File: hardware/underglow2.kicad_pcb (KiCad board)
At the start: 4 copper layers, 60 x 55 mm, 85 parts, among them J101 Conn_ST_STDC14, J102 ZE05H-16DP-2H, Q101 AO3401A, Q102 AO3400A, Q103 AO3400A, Q104 AO3400A, U101 ESP32-C3FH4, U102 SN65HVD230, U103 AMS1117-3.3, Y101 40_Mhz

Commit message: updates
Signed-off-by: Connor Rigby <connorr@hey.com>
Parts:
- added J104: FH34SRJ-6S-0.5SH(50), LCSC_Connector:FFC-SMD_6P-P0.50_FH34SRJ-6S-0.5SH, B.Cu at (48.3, 49.1)
- added SW101: TS-1101-C-W, Button:TS1101CW, B.Cu at (43.6, 55.0)
- added SW104: TS-1101-C-W, Button:TS1101CW, B.Cu at (43.8, 42.5)
- AE101: footprint RF_Antenna:Johanson_2450AT18x100 -> LCSC_Antenna:ANT-SMD_L3.2-W1.6
- H101, H102, H103: value SMTSO2020CTJ -> SMTSO2020CTJ
- U101: footprint Package_DFN_QFN:HVQFN-32-1EP_5x5mm_P0.5mm_EP3.1x3.1mm_ThermalVias -> LCSC_Microcontroller:QFN50P500X500X90-33N
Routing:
- net VDD: track 52.8 -> 62.3 mm, vias 12 -> 15
- net /MTMS: track 90.0 -> 94.6 mm
- net GND: track 69.2 -> 73.3 mm, vias 38 -> 39
- net /MTDI: track 84.7 -> 86.3 mm
- net /MTCK: track 112.8 -> 111.7 mm
- net /MTDO: track 96.8 -> 95.8 mm

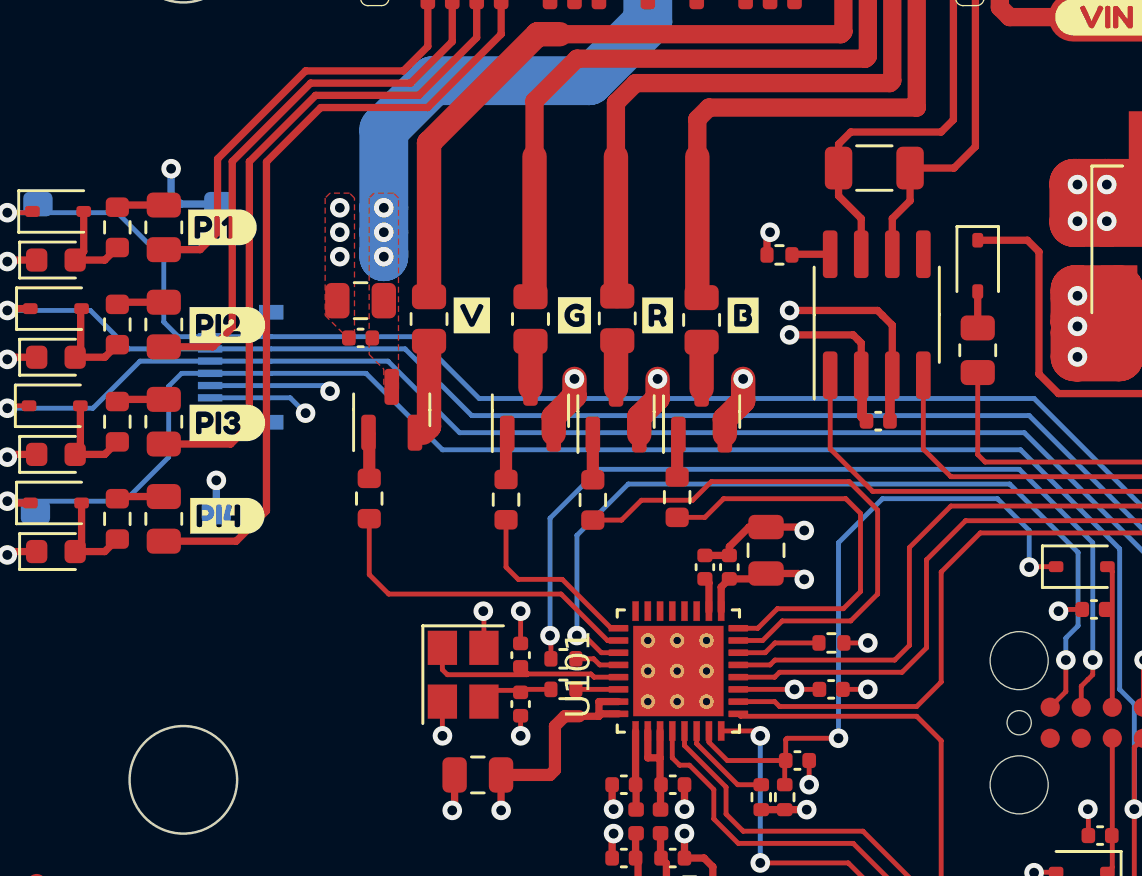
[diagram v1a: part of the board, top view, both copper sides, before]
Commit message: Add 3d render
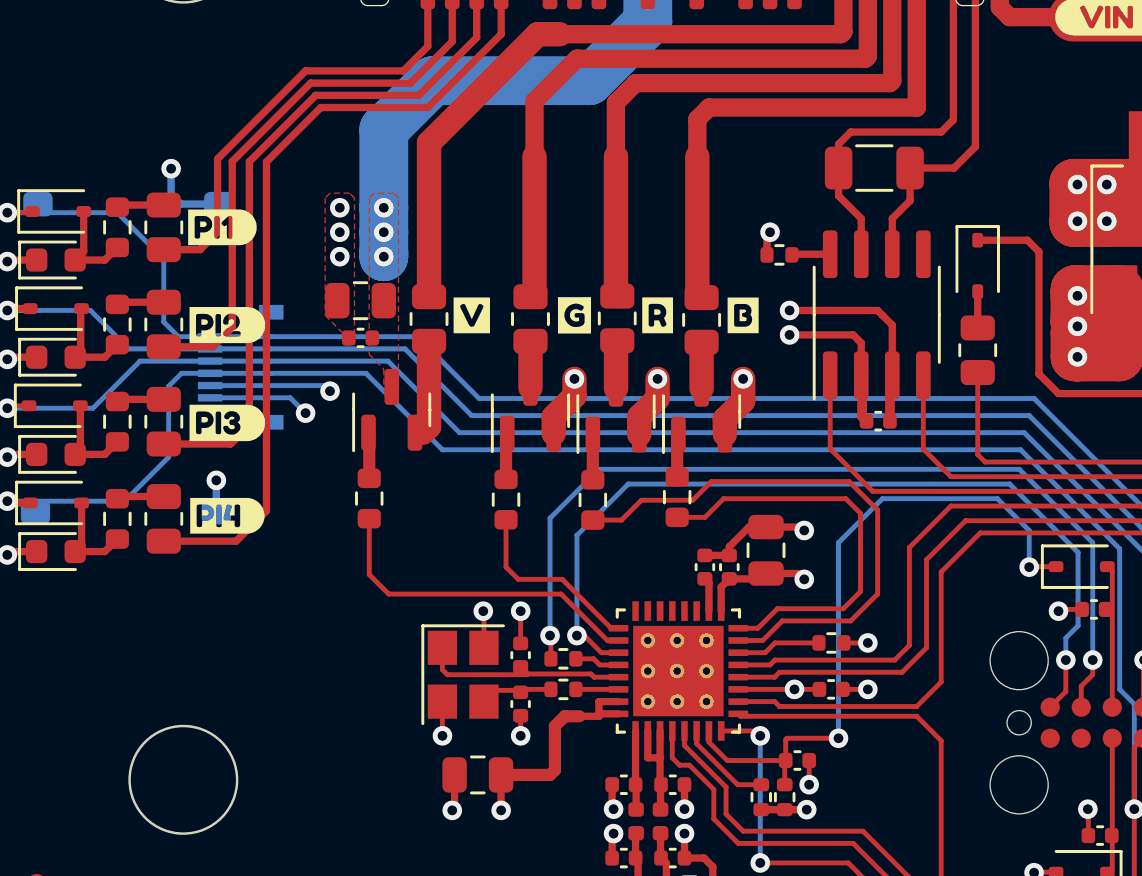
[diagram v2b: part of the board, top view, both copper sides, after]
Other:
- board text added: "PCB3D_BR_Underglow2"
- board text added: "PCB3D_TL_Underglow2"

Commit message: updates
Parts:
- added C1: 22uF, Capacitor_SMD:CP_Elec_4x5.4, F.Cu at (91.2, 42.8)
- added C2: C_0805_10u_X5R, Capacitor_SMD:C_0805_2012Metric, F.Cu at (82.5, 46.1)
- added C3: 4.7uF, Capacitor_SMD:C_0805_2012Metric, F.Cu at (89.3, 39.2)
- added H103: SMTSO2020CTJ, LCSC_Connector:SMTSO2020CTJ, F.Cu at (46.0, 32.0)
- added H103: SMTSO2020CTJ, LCSC_Connector:SMTSO2020CTJ, F.Cu at (46.0, 66.0)
- added H103: SMTSO2020CTJ, LCSC_Connector:SMTSO2020CTJ, F.Cu at (92.0, 73.0)
- added TP1: TestPoint, TestPoint:TestPoint_Pad_D1.5mm, F.Cu at (80.0, 37.2)
- added TP2: TestPoint, TestPoint:TestPoint_Pad_D1.5mm, B.Cu at (89.5, 47.5)
- added TP3: TestPoint, TestPoint:TestPoint_Pad_D1.5mm, B.Cu at (89.5, 50.0)
- added TP4: TestPoint, TestPoint:TestPoint_Pad_D1.0mm, B.Cu at (50.6, 64.3)
- added TP5: TestPoint, TestPoint:TestPoint_Pad_D1.0mm, B.Cu at (50.6, 62.3)
- added TP6: TestPoint, TestPoint:TestPoint_Pad_D1.0mm, B.Cu at (50.6, 60.3)
- added TP7: TestPoint, TestPoint:TestPoint_Pad_D1.0mm, B.Cu at (52.6, 60.3)
- added TP8: TestPoint, TestPoint:TestPoint_Pad_D1.0mm, B.Cu at (52.6, 62.3)
- added TP9: TestPoint, TestPoint:TestPoint_Pad_D1.0mm, B.Cu at (52.6, 64.3)
- added U1: SPX3819M5-L-3-3/TR, Package_TO_SOT_SMD:SOT-23-5, F.Cu at (86.6, 49.0)
- C110: value C_0402_DNP -> C_0402_100nf_X7R
- C116: value C_0805_1u_X7R -> 4.7uF
- C117: value C_0805_1u_X7R -> C_0805_10u_X5R
- FB101: value FerriteBead_Small -> 70mΩ ±25% 330Ω@100MH
- L101: value L_Small -> 2nH
- L102: value L_Small -> 2.2nH
- R121: value R_0402_DNP -> 0R
- U103: value AMS1117-3.3 -> SPX1117M3-L-5-0/TR
- kibuzzard-648F93D4: moved to B.Cu
- moved C116 9.45 mm to (82.5, 48.2), turned to 180 degrees
- moved C107 9.13 mm to (61.5, 63.4), turned to 180 degrees
- moved kibuzzard-648F93D4 9.12 mm to (86.2, 47.5), turned to 180 degrees
- moved FB101 6.25 mm to (93.0, 39.2), turned to 180 degrees
- moved C106 5.14 mm to (61.9, 69.2), turned to -90 degrees
- moved AE101 4.27 mm to (65.0, 72.7), turned to 90 degrees
- moved C117 4.18 mm to (89.8, 49.0), turned to -90 degrees
- moved U103 3.45 mm to (84.0, 40.5)
- moved C120 2.51 mm to (73.5, 66.0), turned to -90 degrees
- moved C108 2.05 mm to (68.1, 69.2), turned to 90 degrees
- moved R123 2.02 mm to (72.5, 66.0)
- moved R124 2.02 mm to (71.5, 66.0)
- moved C114 1.72 mm to (68.8, 56.4), turned to 0 degrees
- moved C113 1.01 mm to (70.8, 56.6)
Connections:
- AE101 pad 1: GND -> /RF_STUB
- C116 pad 1: Net-(U103-VI) -> +5V
- U101 pad 19: unconnected-(U101-SPIHD-Pad19) -> /SPIHD
- U101 pad 20: unconnected-(U101-SPIWP-Pad20) -> /SPIWP
- U101 pad 21: unconnected-(U101-SPICS0-Pad21) -> /SPICS0
- U101 pad 22: unconnected-(U101-SPICLK-Pad22) -> /SPICLK
- U101 pad 23: unconnected-(U101-SPID-Pad23) -> /SPID
- U101 pad 24: unconnected-(U101-SPIQ-Pad24) -> /SPIQ
- U103 pad 2: VDD -> +5V
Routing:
- net /SPIHD: track 0.00 -> 32.2 mm, vias 0 -> 1
- net VS: track 68.1 -> 40.3 mm, vias 6 -> 9
- net /SPIWP: track 0.00 -> 27.1 mm, vias 0 -> 1
- net /SPICS0: track 0.00 -> 21.7 mm, vias 0 -> 1
- net /VCP_TX: track 37.0 -> 56.5 mm
- net /VCP_RX: track 35.5 -> 55.0 mm
- net /SPID: track 0.00 -> 19.4 mm, vias 0 -> 1
- net /SPIQ: track 0.00 -> 19.1 mm, vias 0 -> 1
- net /SPICLK: track 0.00 -> 18.7 mm, vias 0 -> 1
- net VDD: track 62.3 -> 44.3 mm, vias 15 -> 18
- net GND: track 73.3 -> 65.0 mm, vias 39 -> 50
- net Net-(U103-VI): track 5.13 -> 0.00 mm
- net /RF_ANT: track 8.05 -> 3.29 mm
- net /NZR1_OUT: track 83.1 -> 87.2 mm
- net +5V: track 0.00 -> 4.04 mm
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- added copper zone on F.Cu, net +5V
- added copper zone on F.Cu, net /RF_STUB
- added copper zone on B.Cu, net GND
- added copper zone on F.Cu, net Net-(U103-VI)
- added copper zone on F.Cu, net VDD
- added copper zone on B.Cu, net VS

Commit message: Prepare for Production
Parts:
- added J103: ZE05-16DS-HU/R, Harness:ZE05-16DS-HU, F.Cu at (157.0, 33.5)
- added T101: ZE05-2022SCF, Harness:ZE05-2022SCF, F.Cu at (141.1, 44.5)
- added T102: ZE05-2022SCF, Harness:ZE05-2022SCF, F.Cu at (145.7, 44.5)
- added T103: ZE05-2022SCF, Harness:ZE05-2022SCF, F.Cu at (150.2, 44.5)
- added T104: ZE05-2022SCF, Harness:ZE05-2022SCF, F.Cu at (154.8, 44.5)
- added T105: ZE05-2022SCF, Harness:ZE05-2022SCF, F.Cu at (159.4, 44.5)
- added T106: ZE05-2022SCF, Harness:ZE05-2022SCF, F.Cu at (164.1, 44.5)
- added T107: ZE05-2022SCF, Harness:ZE05-2022SCF, F.Cu at (168.7, 44.5)
- added T108: ZE05-2022SCF, Harness:ZE05-2022SCF, F.Cu at (173.2, 44.5)
- added T109: ZE05-2022SCF, Harness:ZE05-2022SCF, F.Cu at (141.3, 61.2)
- added T110: ZE05-2022SCF, Harness:ZE05-2022SCF, F.Cu at (145.9, 61.2)
- added T111: ZE05-2022SCF, Harness:ZE05-2022SCF, F.Cu at (150.5, 61.2)
- added T112: ZE05-2022SCF, Harness:ZE05-2022SCF, F.Cu at (155.1, 61.2)
- added T113: ZE05-2022SCF, Harness:ZE05-2022SCF, F.Cu at (159.7, 61.2)
- added T114: ZE05-2022SCF, Harness:ZE05-2022SCF, F.Cu at (164.3, 61.2)
- added T115: ZE05-2022SCF, Harness:ZE05-2022SCF, F.Cu at (168.9, 61.2)
- added T116: ZE05-2022SCF, Harness:ZE05-2022SCF, F.Cu at (173.5, 61.2)
- C104, C105: value C_0402_DNP -> C_0402_18p_NP0
- C111, C112: value C_0402_DNP -> C_0402_3p3_C0G
- FB101: value 70mΩ ±25% 330Ω@100MH -> 300mΩ ±25% 600Ω@100MHz
- J102: value ZE05H-16DP-2H -> ZE05H-16DP-2H
- R101, R108, R109, R110: value 100 -> R_0805_100
- R103, R114, R117, R118: value 1k -> R_0603_1k
- R104, R105, R106, R107: value 100 -> R_0603_100
- R111: value 220 -> R_0603_220
- R121: value 0R -> R_0402_0
- renumbered H103 to H104
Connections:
- H104 pad 1: unconnected-(H103-Pad1) -> unconnected-(H104-Pad1)
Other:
- board text added: "Harness"

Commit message: submit for production
Signed-off-by: Connor Rigby <connorr@hey.com>
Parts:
- removed the H103 at (46.0, 32.0)
- removed the H103 at (46.0, 66.0)
- removed J103: ZE05-16DS-HU/R, Harness:ZE05-16DS-HU
- removed T101, T102, T103, T104, T105, T106, T107, T108, T109, T110, T111, T112, T113, T114, T115, T116: ZE05-2022SCF, Harness:ZE05-2022SCF
- H101, H102, H103, H104: value SMTSO2020CTJ -> MountingHole; footprint LCSC_Connector:SMTSO2020CTJ -> MountingHole:MountingHole_2.2mm_M2_Pad_Via
- moved C113 0.65 mm to (71.5, 56.6)
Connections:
- H101 pad 1: unconnected-(H101-Pad1) -> GND
- H102 pad 1: unconnected-(H102-Pad1) -> GND
- H103 pad 1: unconnected-(H103-Pad1) -> GND
- H104 pad 1: unconnected-(H104-Pad1) -> GND
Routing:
- net VDD: track 44.3 -> 50.3 mm, vias 18 -> 19
- net /VCP_TX: track 56.5 -> 58.7 mm
- net /VCP_RX: track 55.0 -> 57.1 mm
- net GND: track 65.0 -> 67.0 mm, vias 50 -> 90
- net VS: track 40.3 -> 42.1 mm, vias 9 -> 11
- net /SPIHD: track 32.2 -> 33.9 mm
- net /SPIWP: track 27.1 -> 28.4 mm
- net /MTDO: track 95.8 -> 97.1 mm
- net /SPICS0: track 21.7 -> 22.5 mm
- net /SPICLK: track 18.7 -> 19.4 mm
- net /EN: track 27.9 -> 27.4 mm
- added copper zone on In2.Cu, net GND
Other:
- outline, holes or cut-outs redrawn
- board text removed: "Harness"
